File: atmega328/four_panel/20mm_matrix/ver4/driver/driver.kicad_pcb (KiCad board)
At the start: 2 copper layers, 40 x 40 mm, 88 parts, among them IC1 ATMEGA328P-M, IC2 ATMEGA328P-M, IC3 ATMEGA328P-M, IC4 ATMEGA328P-M, P1 CONN_2X2, P2 CONN_2X2, P3 CONN_2X2, P4 CONN_2X2, U1 DMC2400UV, U10 DMC2400UV, U11 DMC2400UV, U12 DMC2400UV, U13 DMC2400UV, U14 DMC2400UV, U15 DMC2400UV, U16 DMC2400UV, U17 DMC2400UV, U18 DMC2400UV, U19 DMC2400UV, U2 DMC2400UV, U20 DMC2400UV, U21 DMC2400UV, U22 DMC2400UV, U23 DMC2400UV, U24 DMC2400UV, U25 DMC2400UV, U26 DMC2400UV, U27 DMC2400UV, U28 DMC2400UV, U29 DMC2400UV, U3 DMC2400UV, U30 DMC2400UV, U31 DMC2400UV, U32 DMC2400UV, U4 DMC2400UV, U5 DMC2400UV, U6 DMC2400UV, U7 DMC2400UV, U8 DMC2400UV, U9 DMC2400UV, X1 CER_RESO, X2 CER_RESO, X3 CER_RESO, X4 CER_RESO

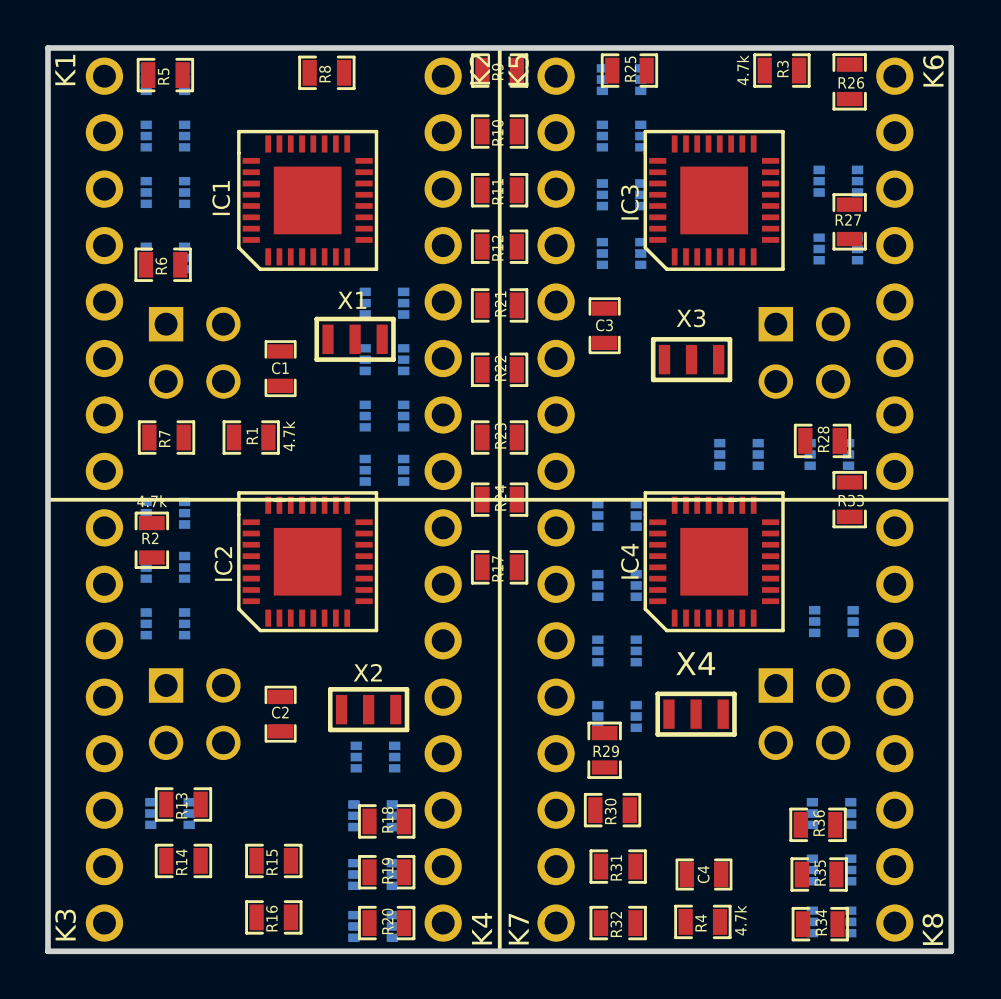
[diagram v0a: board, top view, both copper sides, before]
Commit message: Added version of single matrix atmega328 design with mosfets.
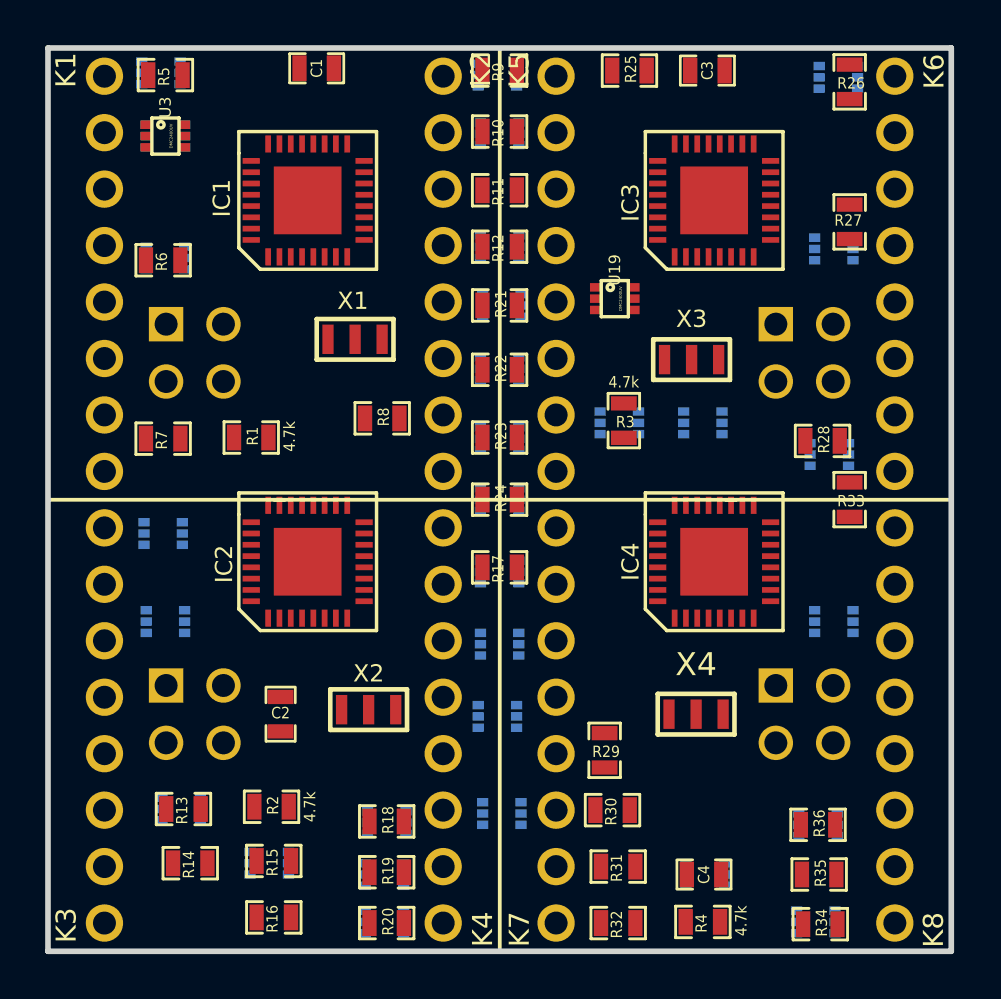
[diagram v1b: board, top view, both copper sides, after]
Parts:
- U19, U3: moved to F.Cu
- moved R3 17.0 mm to (75.5, 66.5), turned to 270 degrees
- moved R8 15.5 mm to (64.8, 66.4), turned to 0 degrees
- moved C1 13.4 mm to (61.9, 50.9), turned to 180 degrees
- moved R2 12.9 mm to (59.9, 83.6), turned to 0 degrees
- moved C3 12.2 mm to (79.2, 51.0), turned to 180 degrees
- moved U11 11.6 mm to (59.8, 86.1)
- moved U13 6.13 mm to (70.1, 83.9)
- moved U32 5.98 mm to (79.1, 86.6)
- moved U17 5.50 mm to (69.9, 51.2)
- moved U20 5.41 mm to (70.0, 58.8)
- moved U18 5.40 mm to (70.0, 53.8)
- moved U28 5.30 mm to (69.9, 79.6)
- moved U8 5.26 mm to (70.0, 70.0)
- moved U26 5.23 mm to (70.0, 73.2)
- moved U27 5.21 mm to (70.0, 76.4)
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
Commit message: Finished initial layout and routing of atmega328 G4 4x20mm matrix driver sub-panel with mosfet.
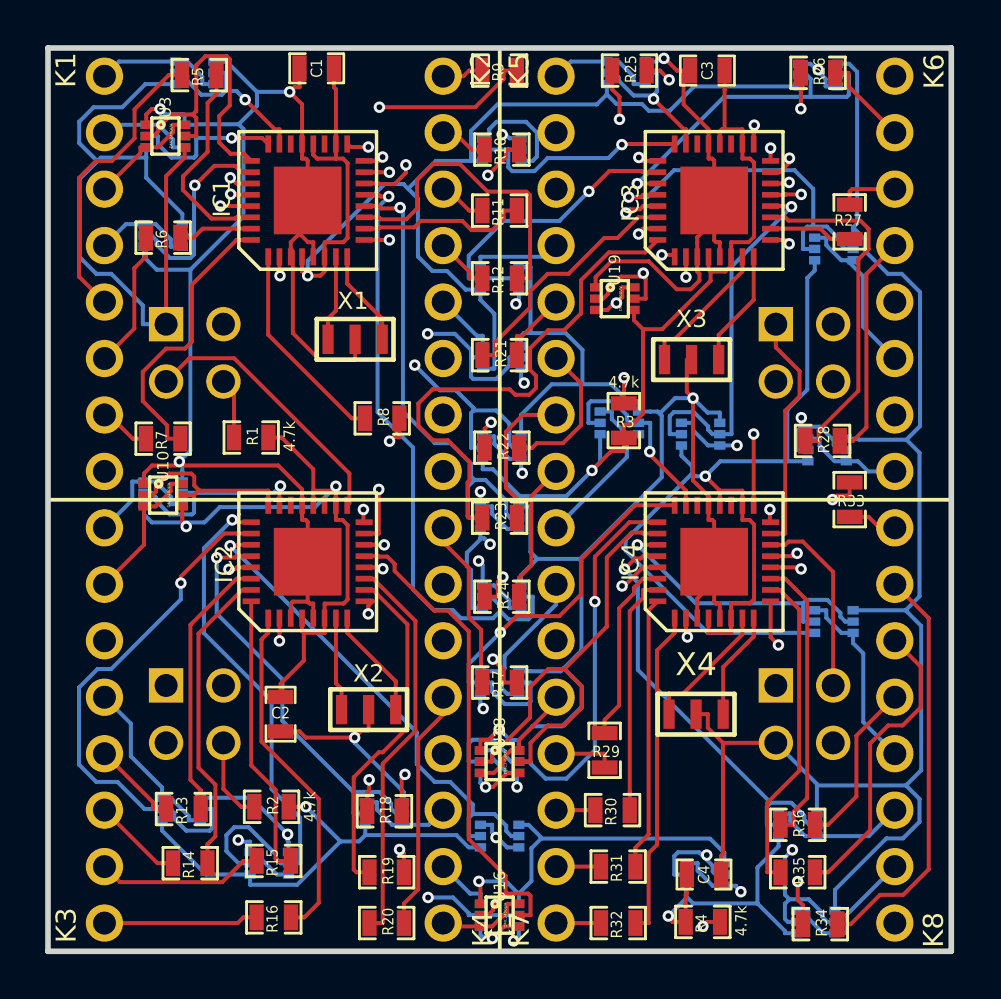
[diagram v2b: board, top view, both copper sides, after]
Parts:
- U10, U16, U28: moved to F.Cu
- moved U17 5.70 mm to (75.6, 51.1)
- moved U10 5.60 mm to (55.1, 69.8)
- moved U15 5.41 mm to (70.0, 88.4)
- moved U27 5.20 mm to (70.0, 81.6)
- moved U16 5.11 mm to (70.0, 88.4)
- moved R17 5.10 mm to (70.0, 78.1)
- moved U26 4.90 mm to (70.0, 78.1)
- moved R24 4.30 mm to (70.1, 74.3)
- moved U8 4.30 mm to (70.1, 74.3)
- moved R23 3.55 mm to (70.0, 70.8)
- moved U6 3.50 mm to (70.1, 67.7)
- moved U7 3.50 mm to (70.0, 70.8)
- moved R22 3.45 mm to (70.1, 67.7)
- moved U5 2.30 mm to (70.1, 63.7)
- moved R21 2.20 mm to (70.0, 63.6)
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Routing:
- net GND: track 0.00 -> 316.8 mm, vias 0 -> 10
- net +5V: track 0.00 -> 310.3 mm, vias 0 -> 11
- net /SCK: track 0.00 -> 67.8 mm, vias 0 -> 3
- net /MISO: track 0.00 -> 65.9 mm, vias 0 -> 4
- net /MOSI: track 0.00 -> 55.1 mm, vias 0 -> 3
- net /RESET_DRV0: track 0.00 -> 50.4 mm, vias 0 -> 3
- net /ROW7_DRV0: track 0.00 -> 28.1 mm, vias 0 -> 1
- net /ROW2_DRV1: track 0.00 -> 24.5 mm, vias 0 -> 1
- net /RESET_DRV3: track 0.00 -> 23.4 mm, vias 0 -> 2
- net /ROW3_DRV1: track 0.00 -> 23.1 mm, vias 0 -> 1
- net /COL2_DRV2: track 0.00 -> 23.1 mm
- net /ROW7_DRV1: track 0.00 -> 22.6 mm
- net /ROW4_DRV1: track 0.00 -> 21.8 mm, vias 0 -> 1
- net /ROW5_DRV0: track 0.00 -> 21.2 mm, vias 0 -> 2
- net /ROW3_DRV3: track 0.00 -> 21.1 mm
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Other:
- copper layers 2 -> 4
- net class Default: via_dia 0.762 -> 0.508; via_drill 0.508 -> 0.254
- rule via_min_drill: 0.508 -> 0.254
- rule via_min_size: 0.762 -> 0.508

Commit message: Added gerber files for new v0.4 version of driver design.
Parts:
- R10, R11, R12, R13, R14, R15, R16, R17, R18, R19, R20, R21, R22, R23, R24, R25, R26, R27, R28, R29, R30, R31, R32, R33, R34, R35, R36, R5, R6, R7, R8, R9: value 180 -> 82
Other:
- board text added: "4-Matrix Atmega328 Driver V0.4 www.iorodeo.com"
- board text removed: "4-Matrix Atmega328 Driver V0.3 www.iorodeo.com"

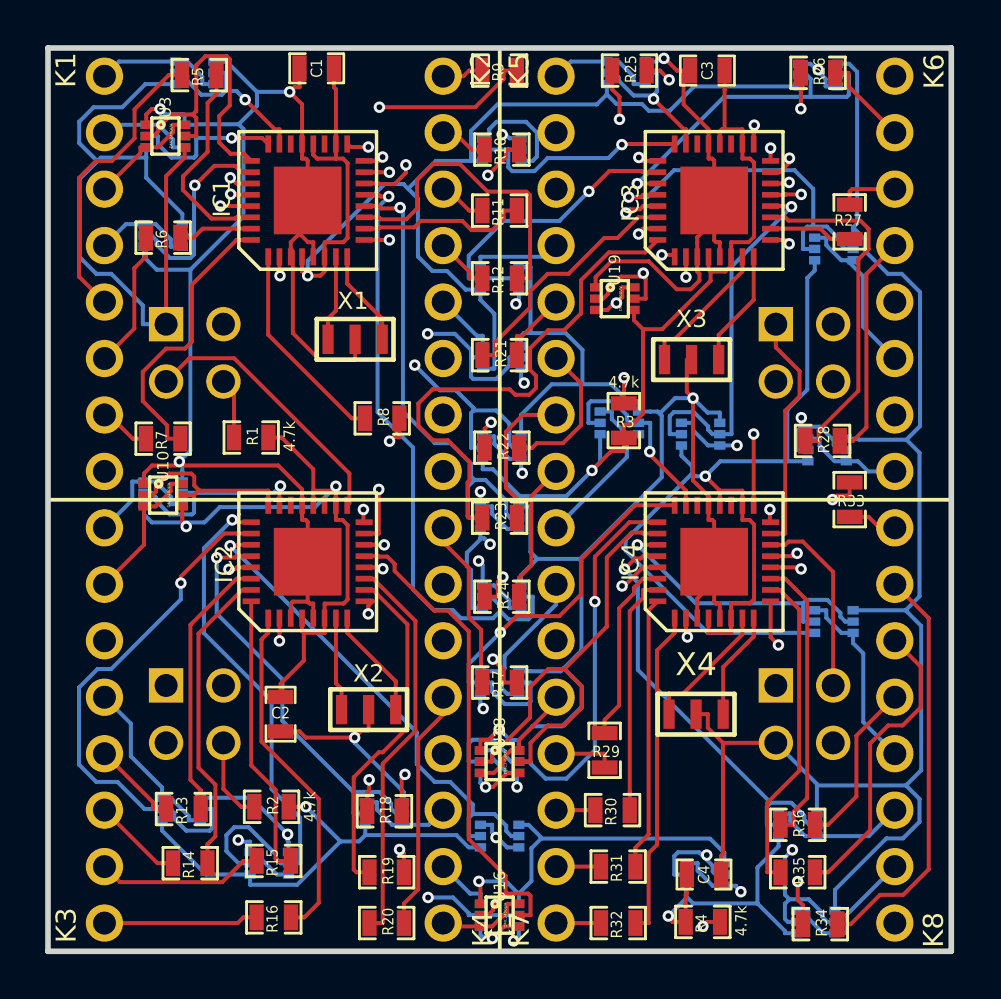
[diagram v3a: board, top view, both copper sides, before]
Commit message: Added revision 2 gerbers for v0.4 of 4x atmega328 driver board.
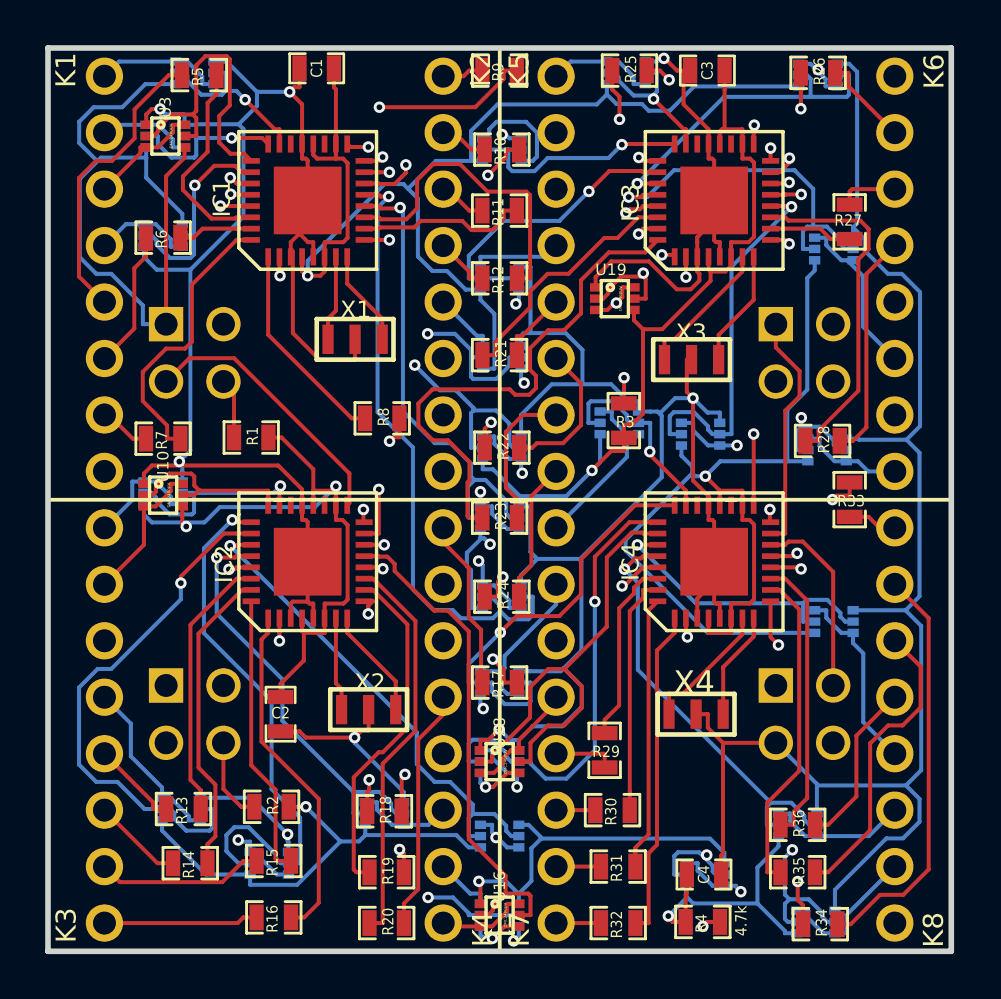
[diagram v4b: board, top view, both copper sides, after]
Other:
- net class Default: clearance 0.1778 -> 0.1016
- rule trace_clearance: 0.1778 -> 0.1016

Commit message: Modified rev 2 or atmega328 driver v0.4.
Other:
- board text added: "4-Matrix Atmega328 Driver V0.4 R2 www.iorodeo.com"
- board text removed: "4-Matrix Atmega328 Driver V0.4 www.iorodeo.com"
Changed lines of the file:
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@@
     (links 337)
     (no_connects 0)
-    (area 49.823399 49.47125 90.212334 90.176601)
+    (area 49.392116 49.47125 90.212334 90.176601)
     (thickness 1.6)
     (drawings 15)
@@
     (pad_to_mask_clearance 0)
     (aux_axis_origin 0 0)
-    (visible_elements FFFFFF7F)
+    (visible_elements FFFFFF3F)
     (pcbplotparams
       (layerselection 284196871)
@@
     (at 63.6 62.9)
     (tags "Resonator, Ceramic")
-    (fp_text reference X1 (at 0.027 -1.305) (layer F.SilkS)
+    (fp_text reference X1 (at 0.027 -1.432) (layer F.SilkS)
       (effects (font (size 0.762 0.762) (thickness 0.1524)))
     )
@@
     (at 64.2 79.3)
     (tags "Resonator, Ceramic")
-    (fp_text reference X2 (at 0.062 -1.195) (layer F.SilkS)
+    (fp_text reference X2 (at -0.065 -1.576) (layer F.SilkS)
       (effects (font (size 0.762 0.762) (thickness 0.1524)))
     )
@@
     (at 78.5 63.8)
     (tags "Resonator, Ceramic")
-    (fp_text reference X3 (at -0.014 -1.189) (layer F.SilkS)
+    (fp_text reference X3 (at -0.014 -1.443) (layer F.SilkS)
       (effects (font (size 0.762 0.762) (thickness 0.1524)))
     )
@@
     (at 78.7 79.5)
     (tags "Resonator, Ceramic")
-    (fp_text reference X4 (at -0.087 -1.395) (layer F.SilkS)
+    (fp_text reference X4 (at -0.087 -1.649) (layer F.SilkS)
       (effects (font (size 1.016 1.016) (thickness 0.2032)))
     )
@@
     (descr "Double rangee de contacts 2 x 2 pins")
     (tags CONN)
-    (fp_text reference P3 (at -1.458 -3.429) (layer B.SilkS)
+    (fp_text reference P3 (at -1.204 -3.2766) (layer B.SilkS)
       (effects (font (size 1.016 1.016) (thickness 0.2032)) (justify mirror))
     )
@@
   (module DMC2400UV (layer B.Cu)
     (at 70.1 54.5 270)
-    (fp_text reference U18 (at -1.287 -0.004 360) (layer B.SilkS)
+    (fp_text reference U18 (at -1.2362 0.0214 360) (layer B.SilkS)
       (effects (font (size 0.508 0.508) (thickness 0.1016)) (justify mirror))
     )
@@
   (module DMC2400UV (layer F.Cu)
     (at 70 81.6 270)
-    (fp_text reference U28 (at -1.27 0 270) (layer F.SilkS)
+    (fp_text reference U28 (at -1.209 0.023 360) (layer F.SilkS)
       (effects (font (size 0.508 0.508) (thickness 0.1016)))
     )
@@
   (module DMC2400UV (layer B.Cu)
     (at 70 60.2 270)
-    (fp_text reference U20 (at -1.272 0.023 360) (layer B.SilkS)
+    (fp_text reference U20 (at -1.1704 0.023 360) (layer B.SilkS)
       (effects (font (size 0.508 0.508) (thickness 0.1016)) (justify mirror))
     )
@@
   (module DMC2400UV (layer B.Cu)
     (at 56.5 51.1 270)
-    (fp_text reference U1 (at 0 1.7 270) (layer B.SilkS)
+    (fp_text reference U1 (at -0.0206 1.5598 270) (layer B.SilkS)
       (effects (font (size 0.508 0.508) (thickness 0.1016)) (justify mirror))
     )
@@
   (module DMC2400UV (layer F.Cu)
     (at 70 88.4 270)
-    (fp_text reference U16 (at -1.27 0 270) (layer F.SilkS)
+    (fp_text reference U16 (at -1.2272 0.023 360) (layer F.SilkS)
       (effects (font (size 0.508 0.508) (thickness 0.1016)))
     )
@@
   (module DMC2400UV (layer B.Cu)
     (at 70 88.4 270)
-    (fp_text reference U15 (at -1.278 -0.104 360) (layer B.SilkS)
+    (fp_text reference U15 (at -1.2272 -0.0024 360) (layer B.SilkS)
       (effects (font (size 0.508 0.508) (thickness 0.1016)) (justify mirror))
     )
@@
   (module DMC2400UV (layer B.Cu)
     (at 64.9 83.9 270)
-    (fp_text reference U14 (at -1.223 0.003 360) (layer B.SilkS)
+    (fp_text reference U14 (at -1.1722 0.0284 360) (layer B.SilkS)
       (effects (font (size 0.508 0.508) (thickness 0.1016)) (justify mirror))
     )
@@
   (module DMC2400UV (layer F.Cu)
     (at 55.1 69.8 270)
-    (fp_text reference U10 (at -1.27 0 270) (layer F.SilkS)
+    (fp_text reference U10 (at 1.32 0.109 360) (layer F.SilkS)
       (effects (font (size 0.508 0.508) (thickness 0.1016)))
     )
@@
   (module DMC2400UV (layer B.Cu)
     (at 70.1 63.7 270)
-    (fp_text reference U5 (at -1.216 -0.004 360) (layer B.SilkS)
+    (fp_text reference U5 (at -1.1652 0.0214 360) (layer B.SilkS)
       (effects (font (size 0.508 0.508) (thickness 0.1016)) (justify mirror))
     )
@@
   (module DMC2400UV   placed (layer F.Cu)
     (at 55.2 53.9 270)
-    (fp_text reference U3 (at -1.27 0 270) (layer F.SilkS)
+    (fp_text reference U3 (at -1.195 -0.045 360) (layer F.SilkS)
       (effects (font (size 0.508 0.508) (thickness 0.1016)))
     )
@@
     (effects (font (size 0.889 0.889) (thickness 0.2032)))
   )
-  (gr_text K7 (at 70.8787 89.027 90) (layer F.SilkS)
+  (gr_text K7 (at 70.993 85.725 90) (layer F.SilkS)
     (effects (font (size 0.889 0.889) (thickness 0.2032)))
   )
@@
     (effects (font (size 0.889 0.889) (thickness 0.2032)))
   )
-  (gr_text K5 (at 70.866 50.9905 90) (layer F.SilkS)
+  (gr_text K5 (at 70.866 52.6796 90) (layer F.SilkS)
     (effects (font (size 0.889 0.889) (thickness 0.2032)))
   )
-  (gr_text K4 (at 69.2531 89.027 90) (layer F.SilkS)
+  (gr_text K4 (at 69.215 85.725 90) (layer F.SilkS)
     (effects (font (size 0.889 0.889) (thickness 0.2032)))
   )
@@
     (effects (font (size 0.889 0.889) (thickness 0.2032)))
   )
-  (gr_text K2 (at 69.1642 50.9524 90) (layer F.SilkS)
+  (gr_text K2 (at 69.3166 52.705 90) (layer F.SilkS)
     (effects (font (size 0.889 0.889) (thickness 0.2032)))
   )
@@
     (effects (font (size 0.889 0.889) (thickness 0.2032)))
   )
-  (gr_text "4-Matrix Atmega328 Driver V0.4\nwww.iorodeo.com" (at 63.5 70 90) (layer B.SilkS)
+  (gr_text "4-Matrix Atmega328 Driver V0.4 R2\nwww.iorodeo.com" (at 62.484 65.7606 90) (layer B.SilkS)
     (effects (font (size 1.016 1.016) (thickness 0.2032)) (justify mirror))
   )
